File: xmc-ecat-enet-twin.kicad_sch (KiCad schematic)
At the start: 1 part

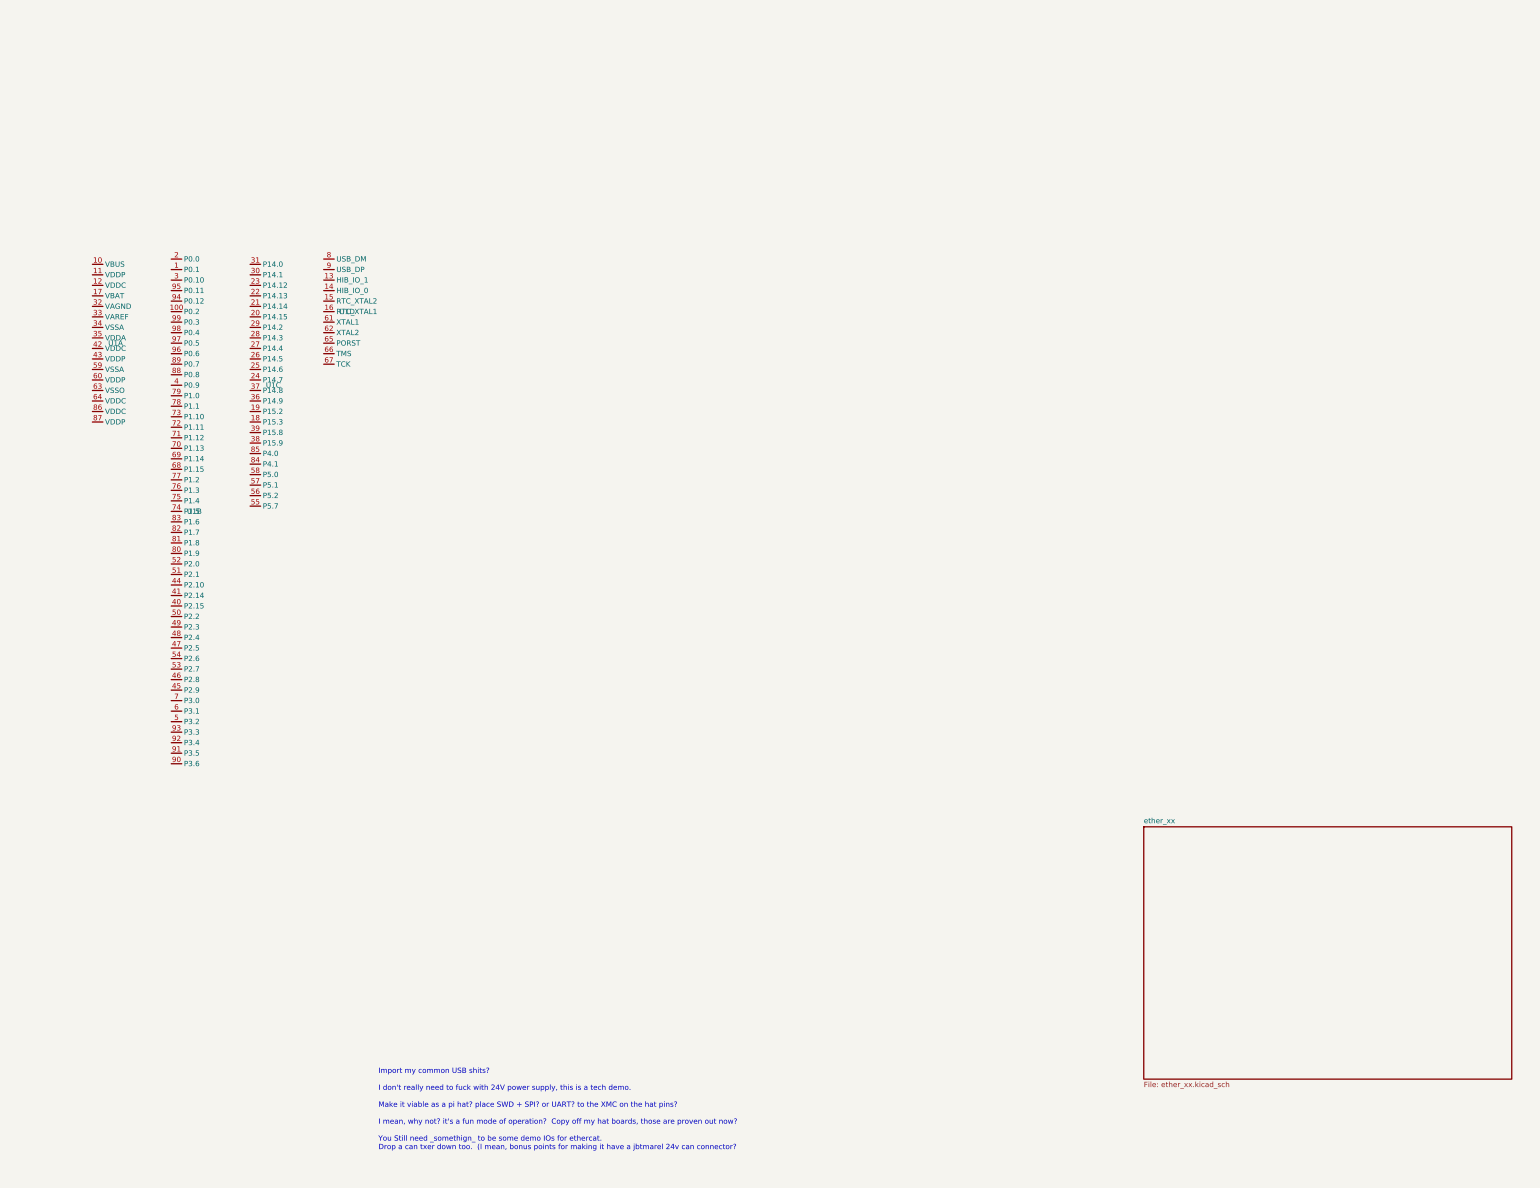
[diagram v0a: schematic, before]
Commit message: sketching continues
You cannot do MII on F100 package, so don't even try on the F144,
there's no saving vs the E196.

Start stuffing in what else you'd actually need for this.  Give it a pi
interface to use as a daughterboard, usb to use standalone, jbt marel
can to use there,

always underestimate just how much _stuff_ there is to do though...
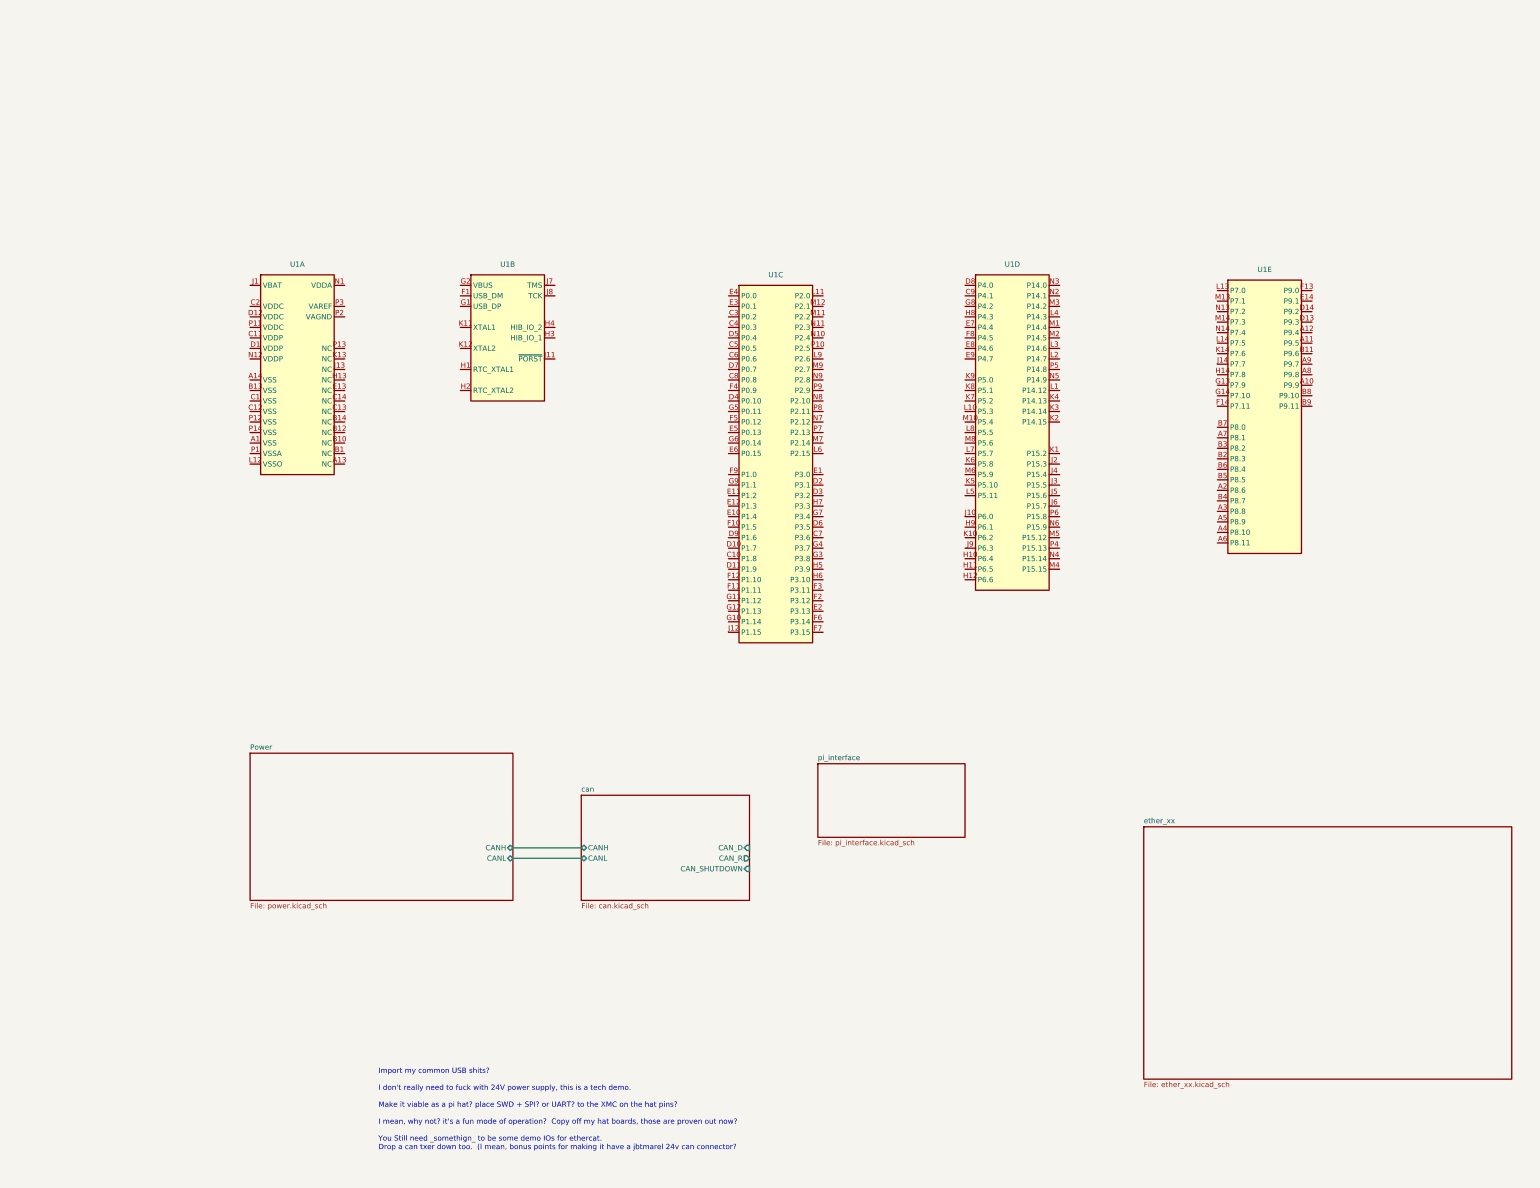
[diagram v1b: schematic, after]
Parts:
- removed U1: (no value), symbol karl-parts:XMC4800_F100x
- added U1: (no value), KPackage_BGA:LFBGA-196_14x14_P0.8mm, symbol karl-parts:XMC4800_E196x
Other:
- added sheet Power (power.kicad_sch)
- added sheet can (can.kicad_sch)
- added sheet pi_interface (pi_interface.kicad_sch)

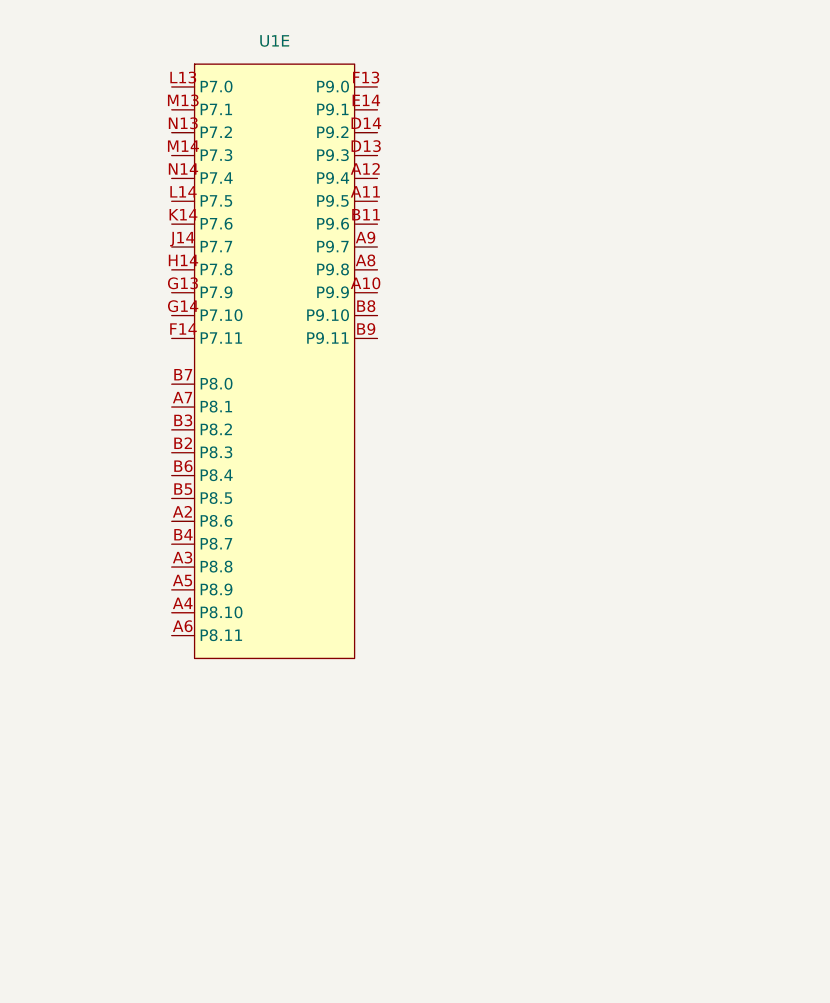
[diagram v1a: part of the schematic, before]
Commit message: finish the tism on magnetics.
jsut use H110X symbol numbering and any H110x footprint, they're all the
same.
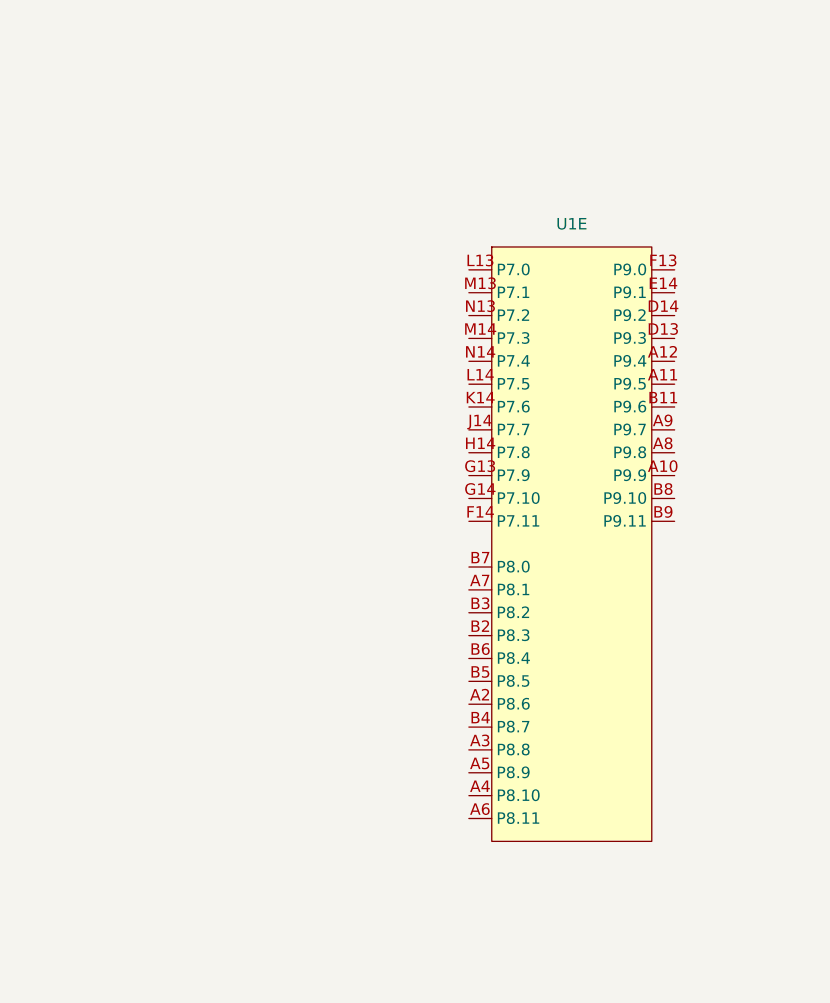
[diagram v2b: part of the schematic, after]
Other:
- moved on the sheet: U1E
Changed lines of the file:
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@@
 	(symbol
 		(lib_id "karl-parts:XMC4800_E196x")
-		(at 317.5 38.1 0)
+		(at 350.52 58.42 0)
 		(unit 5)
 		(body_style 1)
@@
 		(fields_autoplaced yes)
 		(property "Reference" "U1"
-			(at 326.39 35.56 0)
+			(at 359.41 55.88 0)
 			(show_name no)
 			(do_not_autoplace no)
@@
 		)
 		(property "Value" ""
-			(at 317.5 38.1 0)
+			(at 350.52 58.42 0)
 			(show_name no)
 			(do_not_autoplace no)
@@
 		)
 		(property "Footprint" "KPackage_BGA:LFBGA-196_14x14_P0.8mm"
-			(at 317.5 38.1 0)
+			(at 350.52 58.42 0)
 			(hide yes)
 			(show_name no)
@@
 		)
 		(property "Datasheet" ""
-			(at 317.5 38.1 0)
+			(at 350.52 58.42 0)
 			(hide yes)
 			(show_name no)
@@
 		)
 		(property "Description" ""
-			(at 317.5 38.1 0)
+			(at 350.52 58.42 0)
 			(hide yes)
 			(show_name no)

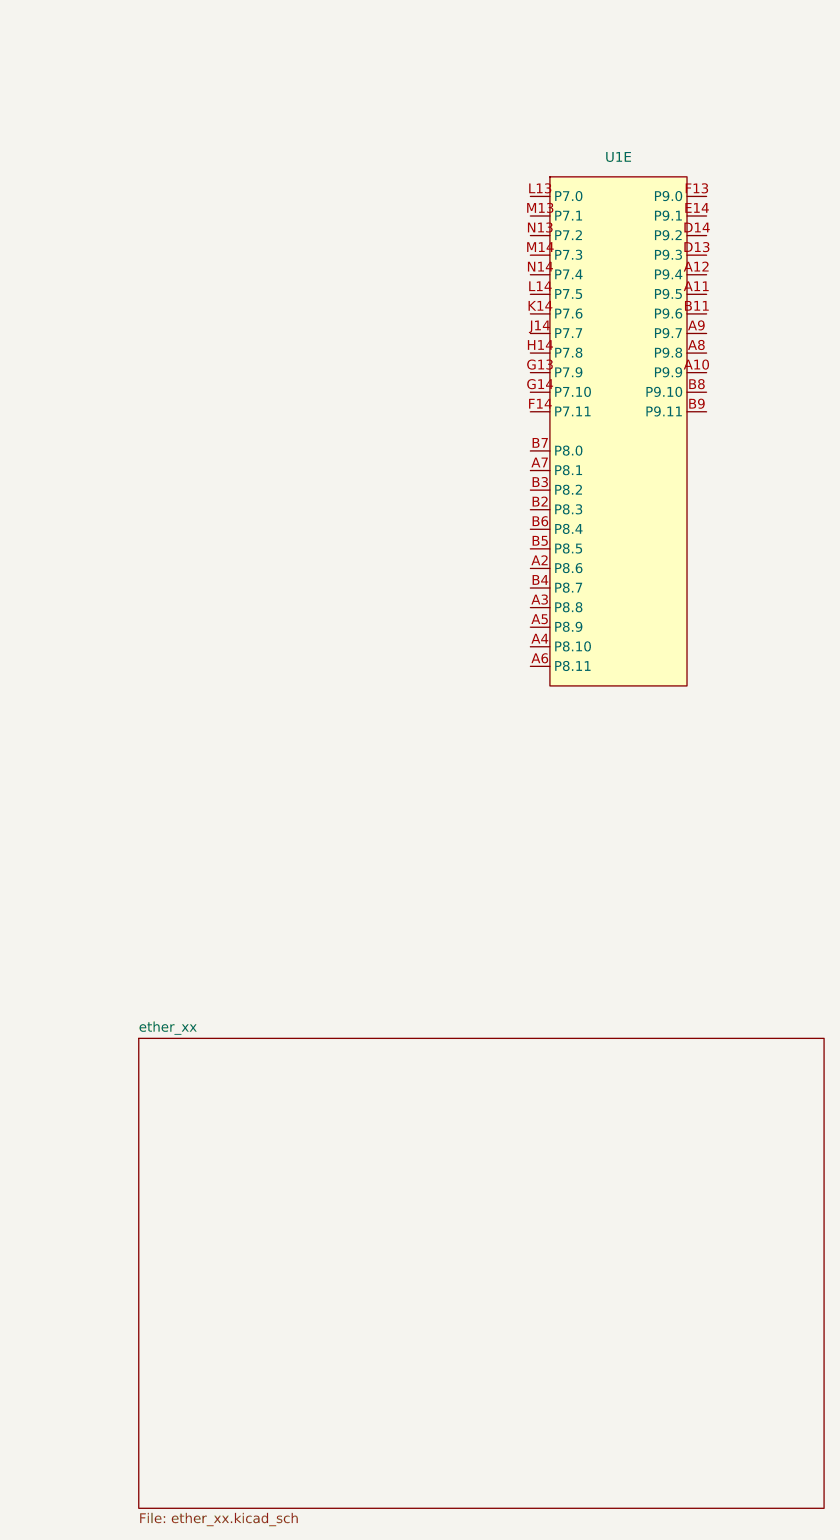
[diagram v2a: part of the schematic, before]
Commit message: ether: switch phys, confirm magnetics, start wiring
Moved from LAN8710 to RTL8201 for the phys.  voltage mode instead of
current mode so less hassle getting them up, and less parts.  Also
cheaper, and realllly well supported too, so, all good.  Had to make a
symbol, but that's not realllly a big deal right?

We've locked in the arrangement and footprint for the magnetics now too
at least, after our research tear on them.

We've mostly figured out heirarchical bus symbols too I think...
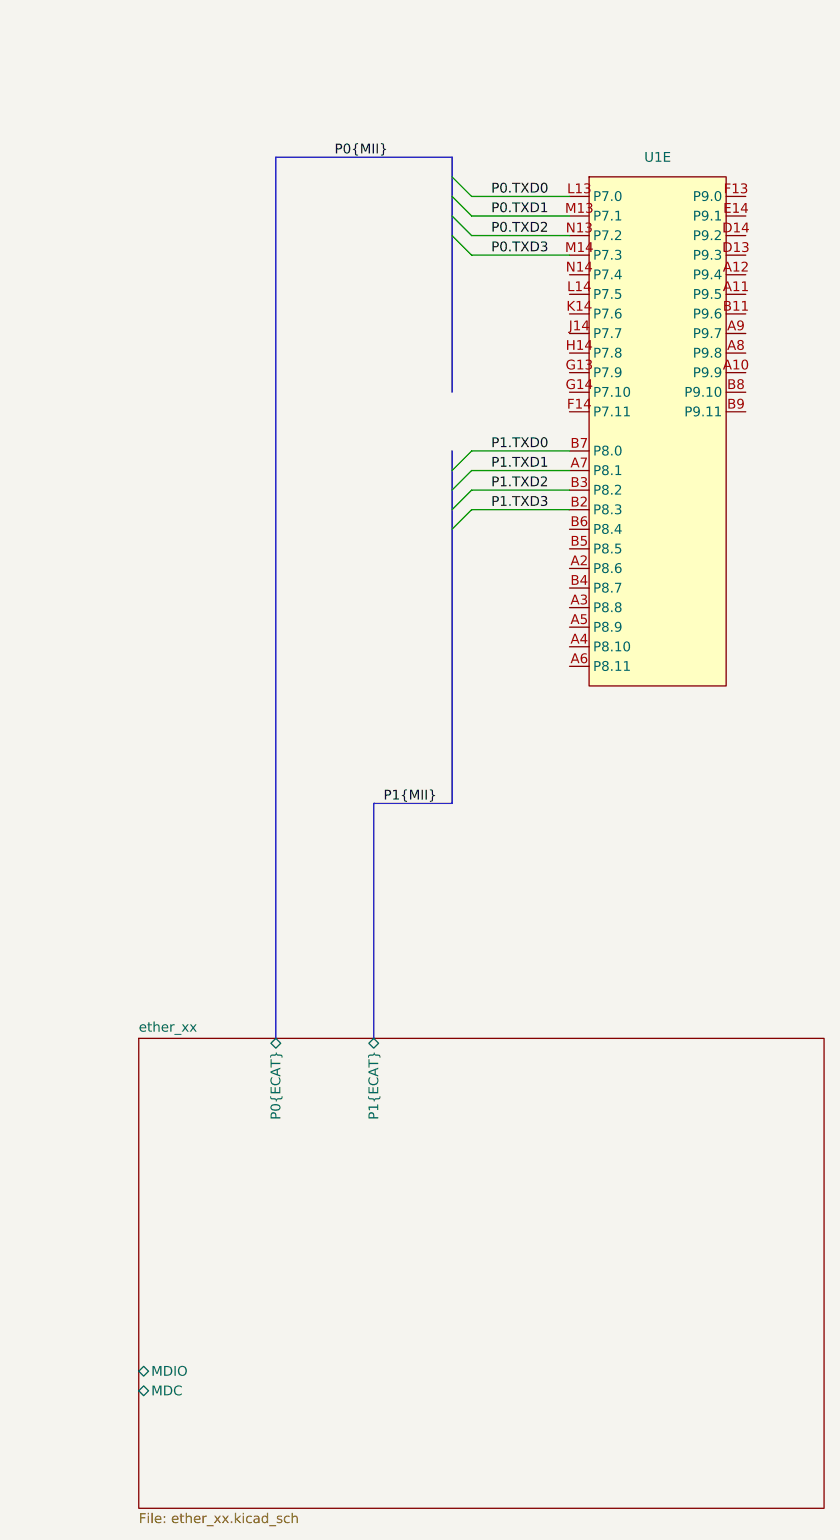
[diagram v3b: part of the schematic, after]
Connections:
- net P1.TXD1: now reaches U1.A7 (P8.1)
- net P1.TXD3: now reaches U1.B2 (P8.3)
- net P1.TXD2: now reaches U1.B3 (P8.2)
- net P1.TXD0: now reaches U1.B7 (P8.0)
- net P0.TXD0: now reaches U1.L13 (P7.0)
- net P0.TXD1: now reaches U1.M13 (P7.1)
- net P0.TXD3: now reaches U1.M14 (P7.3)
- net P0.TXD2: now reaches U1.N13 (P7.2)
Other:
- sheet ether_xx ports: added MDC, MDIO, P0{ECAT}, P1{ECAT}; removed none
- moved on the sheet: U1E

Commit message: continue with the phys, add debug, hook more up
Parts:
- removed unit 2 of U1
- removed unit 1 of U1
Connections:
- net JTAG_TDO: now reaches U1.M12 (P2.1)
- net P1.RXD2: now reaches U1.A2 (P8.6)
- net P1.TX_ENA: now reaches U1.A3 (P8.8)
- net P1.RX_CLK: now reaches U1.A4 (P8.10)
- net P1.RX_ERR: now reaches U1.A5 (P8.9)
- net P1.RX_DVC: now reaches U1.A6 (P8.11)
- net P1.RXD3: now reaches U1.B4 (P8.7)
- net P1.RXD1: now reaches U1.B5 (P8.5)
- net P1.RXD0: now reaches U1.B6 (P8.4)
- net PHY_RST_N: now reaches U1.D14 (P9.2)
- net P0.TX_CLK: now reaches U1.E14 (P9.1)
- net P1.TX_CLK: now reaches U1.F13 (P9.0)
- net P0.RX_DVC: now reaches U1.F14 (P7.11)
- net P0.RX_ERR: now reaches U1.G13 (P7.9)
- net P0.RX_CLK: now reaches U1.G14 (P7.10)
- net P0.TX_ENA: now reaches U1.H14 (P7.8)
- net P0.RXD3: now reaches U1.J14 (P7.7)
- net P0.RXD2: now reaches U1.K14 (P7.6)
- net P0.RXD1: now reaches U1.L14 (P7.5)
- net P0.RXD0: now reaches U1.N14 (P7.4)
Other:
- added sheet mcu_pwr_debug (mcu_pwr_dbg.kicad_sch)
- sheet ether_xx ports: added P0{MII}, P1{MII}, PHY_25M_IN, PHY_RESET; removed P0{ECAT}, P1{ECAT}
- moved on the sheet: U1C, U1D

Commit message: connect the dots!
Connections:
- net ETH.TXD0: now reaches U1.C5 (P0.5)
- net ETH.TXD1: now reaches U1.C6 (P0.6)
- net ETH.MDIO: now reaches U1.F11 (P1.11)
- net ETH.MDC: now reaches U1.F12 (P1.10)
- net ETH.TX_ENA: now reaches U1.G11 (P1.12)
- net ETH.RX_CLK: now reaches U1.H11 (P6.5)
- net ETH.TX_CLK: now reaches U1.H12 (P6.6)
- net ETH.TXD3: now reaches U1.H9 (P6.1)
- net ETH.TXD2: now reaches U1.J10 (P6.0)
- net ETH.RXD2: now reaches U1.K6 (P5.8)
- net ETH.RX_DVC: now reaches U1.K7 (P5.2)
- net ETH.RXD1: now reaches U1.K8 (P5.1)
- net ETH.RXD0: now reaches U1.K9 (P5.0)
- net ETH.RX_ERR: now reaches U1.L10 (P5.3)
- net ETH.RXD3: now reaches U1.M6 (P5.9)
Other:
- note added: "Do I need CRS/COL for plain ethernet? I don't think so. CRS/DV is combined on RMII, no-one uses COL?"
